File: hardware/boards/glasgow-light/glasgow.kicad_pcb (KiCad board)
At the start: 2 copper layers, 171 parts, among them J1 USB_C_USB2.0, J10 AUX, J2 IDC-Header_2x5_P2.54mm, J3 IDC-Header_2x5_P2.54mm, J4 Conn_01x02, U10 SN74LVC1T45DCKR, U11 SN74LVC1T45DCKR, U12 INA180A2, U15 TPD3S014, U16 SN74LVC1T45DCKR, U17 SN74LVC1T45DCKR, U18 SN74LVC1T45DCKR, U19 PCA6408APW, U31 TPS73101DBV, U36 TLV73312PQDRVR, U4 SN74LVC1T45DCKR, U5 ICE40UP5K-SG48ITR, U6 SN74LVC1T45DCKR, U7 GD32VF103, U8 TLV75533PDRVR, U9 SN74LVC1T45DCKR, Y1 8M

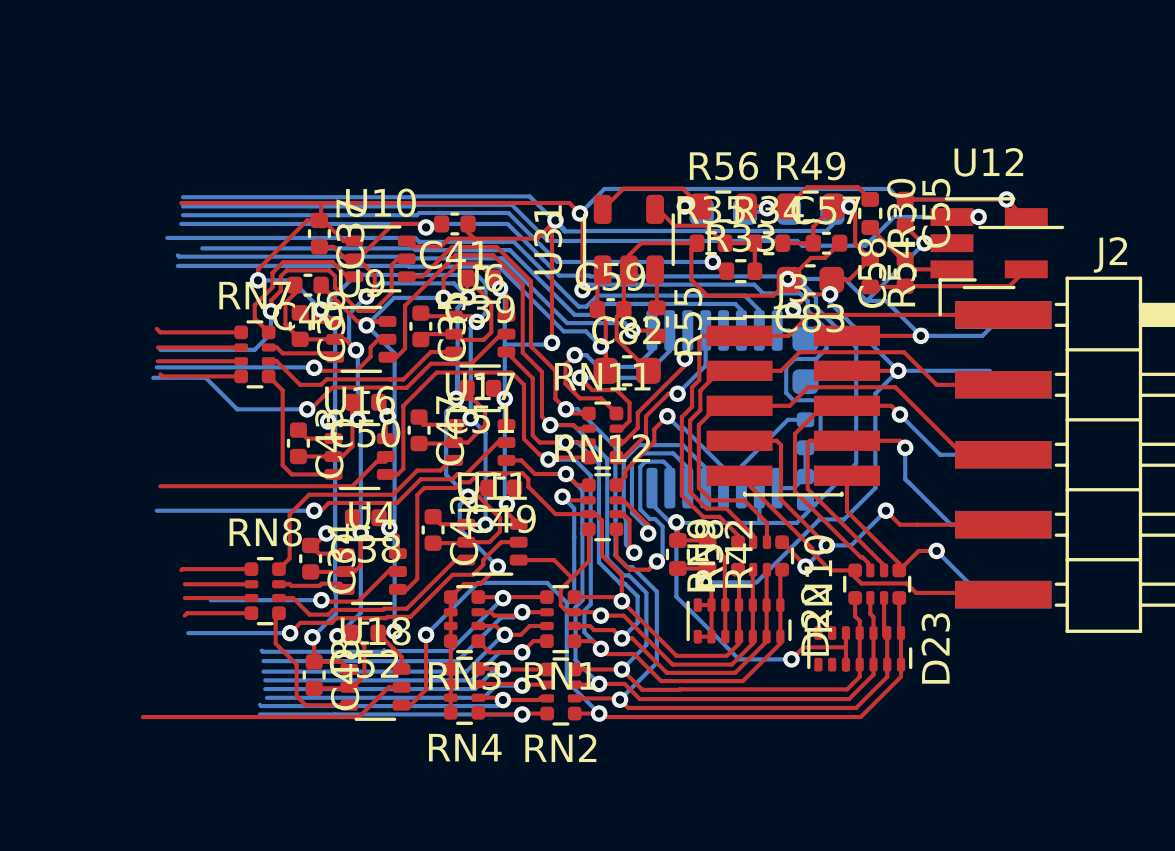
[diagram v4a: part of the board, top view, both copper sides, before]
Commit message: increase width of supply lines
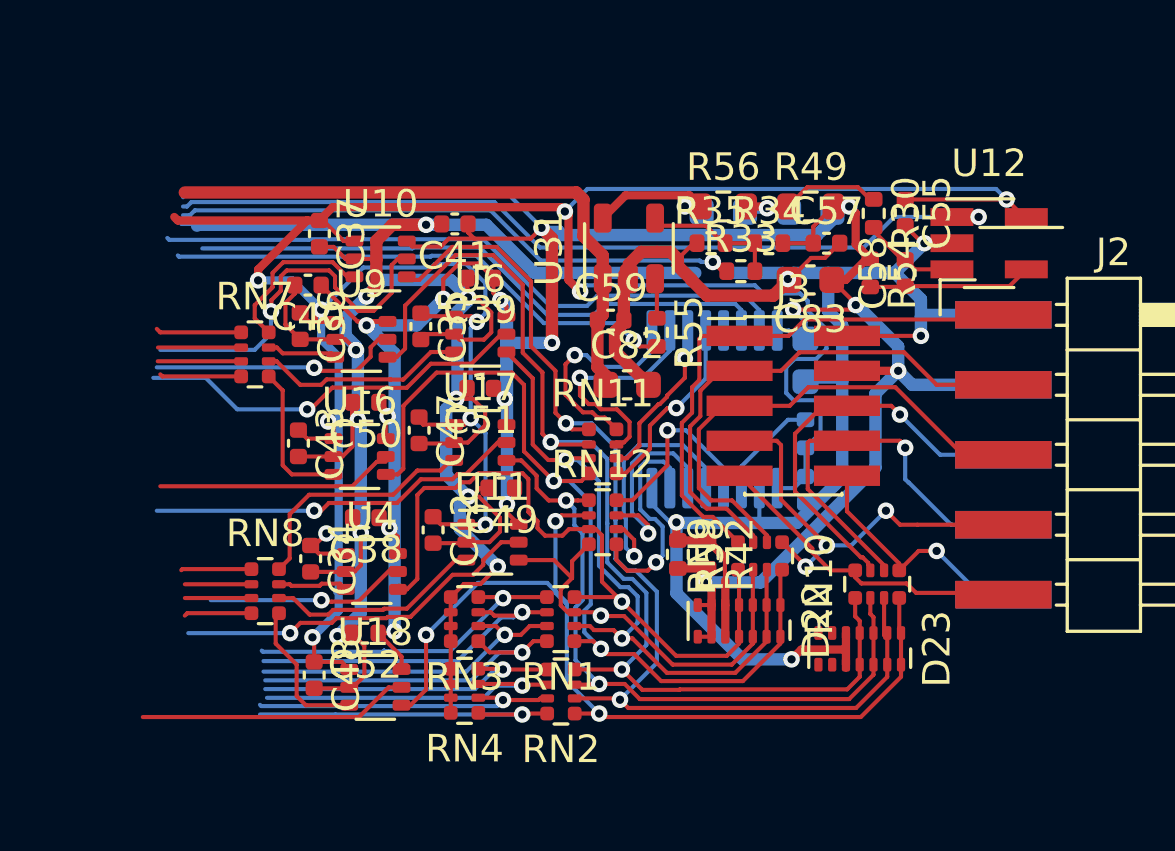
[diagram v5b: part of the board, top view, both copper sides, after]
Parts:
- moved RN11 0.58 mm to (157.4, 43.9)
- moved RN12 0.55 mm to (157.4, 46.5)
- moved C82 0.51 mm to (158.3, 41.5)
- moved C59 0.38 mm to (157.7, 39.2)
- moved R55 0.38 mm to (159.4, 39.6)
- moved U31 0.32 mm to (158.4, 36.6)
- moved R30 0.13 mm to (167.3, 35.3)
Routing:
- net /IO_Banks/VIOA: track 119.3 -> 150.2 mm
- net GND: track 169.1 -> 190.7 mm
- net +3V3: track 109.2 -> 115.3 mm
- net /IO_Banks/IO_Buffer_A/Y0: track 25.1 -> 25.9 mm
- net /IO_Banks/IO_Buffer_A/Y1: track 16.4 -> 15.7 mm
- net /IO_Banks/IO_Buffer_A/Y7: track 34.4 -> 33.7 mm
- net /IO_Banks/IO_Buffer_A/P6: track 5.28 -> 5.96 mm
- net /IO_Banks/IO_Buffer_A/P7: track 6.30 -> 6.91 mm
- net /IO_Banks/IO_Buffer_A/P5: track 7.83 -> 8.42 mm
- net +5V: track 21.4 -> 21.8 mm, vias 1 -> 0

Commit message: add some test points
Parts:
- removed D14: CDSOD323-T36S, Glasgow:D_SOD-323
- removed D5: RED, LED_SMD:LED_0603_1608Metric
- removed R13, R14: 20k, Resistor_SMD:R_0402_1005Metric
- removed R16: 10k, Resistor_SMD:R_0402_1005Metric
- added TP22: 3V3, TestPoint:TestPoint_Pad_D1.0mm, B.Cu at (172.5, 35.3)
- added TP23: VCURR, TestPoint:TestPoint_Pad_D1.0mm, B.Cu at (170.4, 35.3)
- added TP24: GND, TestPoint:TestPoint_Pad_D1.0mm, B.Cu at (170.4, 37.3)
- added TP25: VIO, TestPoint:TestPoint_Pad_D1.0mm, B.Cu at (172.5, 37.3)
- added TP26: Y5, TestPoint:TestPoint_Pad_D1.0mm, B.Cu at (160.0, 52.6)
- added TP27: Y6, TestPoint:TestPoint_Pad_D1.0mm, B.Cu at (160.0, 50.5)
- added TP28: Y7, TestPoint:TestPoint_Pad_D1.0mm, B.Cu at (162.1, 52.6)
- added TP29: ADC7, TestPoint:TestPoint_Pad_D1.0mm, B.Cu at (155.6, 53.2)
- added TP30: ADC5, TestPoint:TestPoint_Pad_D1.0mm, B.Cu at (155.3, 50.5)
- added TP31: GND, TestPoint:TestPoint_Pad_D1.0mm, B.Cu at (162.1, 50.5)
- added TP32: P5, TestPoint:TestPoint_Pad_D1.0mm, B.Cu at (157.9, 41.4)
- added TP33: P7, TestPoint:TestPoint_Pad_D1.0mm, B.Cu at (157.9, 43.4)
- TP4, TP5: moved to B.Cu
- moved J4 160.1 mm to (193.2, 103.5)
- moved J10 126.9 mm to (161.4, 110.9)
- moved TP5 119.8 mm to (155.4, 38.2)
- moved TP4 119.6 mm to (155.2, 41.3)
- moved R1 92.6 mm to (156.2, 39.1), turned to 90 degrees
- moved R2 90.9 mm to (155.8, 37.0), turned to 90 degrees
- moved R6 61.9 mm to (132.3, 87.4)
- moved C30 54.0 mm to (132.1, 83.6)
- moved C31 52.9 mm to (132.0, 79.1)
- moved C22 52.8 mm to (131.8, 74.7)
- moved C11 49.0 mm to (110.6, 53.5)
- moved C12 49.0 mm to (112.6, 57.3)
- moved R22 47.8 mm to (188.8, 75.8)
- moved R21 47.3 mm to (188.6, 63.6)
- moved C21 45.5 mm to (125.7, 85.7)
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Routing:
- net /IO_Banks/IO_Buffer_A/Y7: track 33.7 -> 38.9 mm
- net /IO_Banks/IO_Buffer_A/Y5: track 25.7 -> 29.1 mm
- net GND: track 190.7 -> 194.1 mm
- net /IO_Banks/VIOA: track 150.2 -> 153.2 mm, vias 15 -> 16
- net /SCL: track 21.6 -> 24.3 mm, vias 0 -> 2
- net /IO_Banks/IO_Buffer_A/P7: track 6.91 -> 9.58 mm
- net ADC5: track 12.0 -> 14.2 mm
- net +3V3: track 115.3 -> 117.0 mm
- net ADC7: track 12.1 -> 13.3 mm
- net VIO_CURRENT: track 31.1 -> 32.3 mm
- net /SDA: track 23.7 -> 24.3 mm, vias 0 -> 1

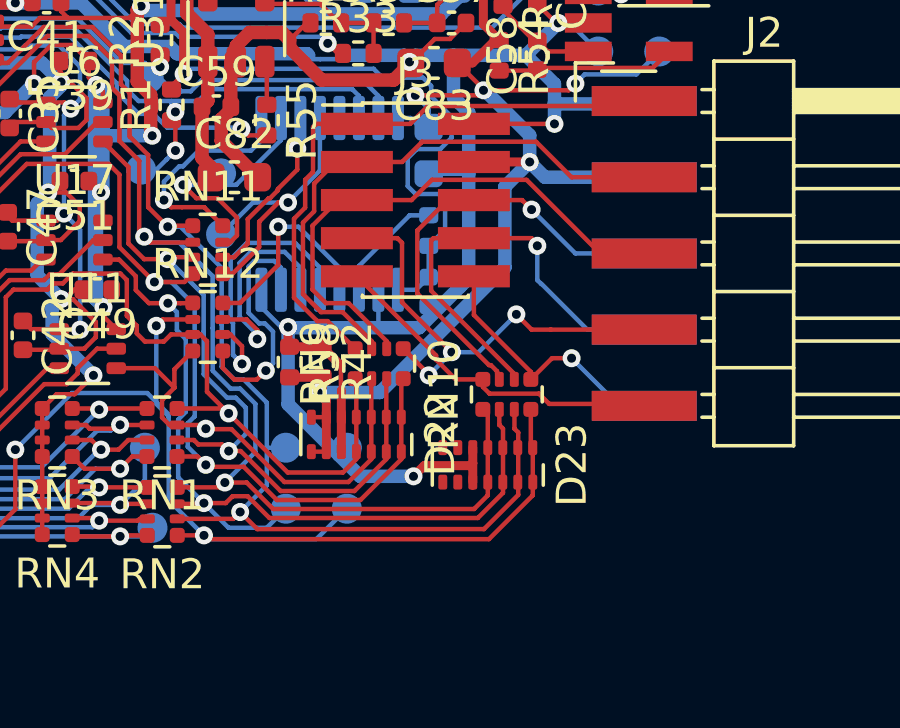
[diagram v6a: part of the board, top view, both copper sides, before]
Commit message: add LEDs for VIO and Y7
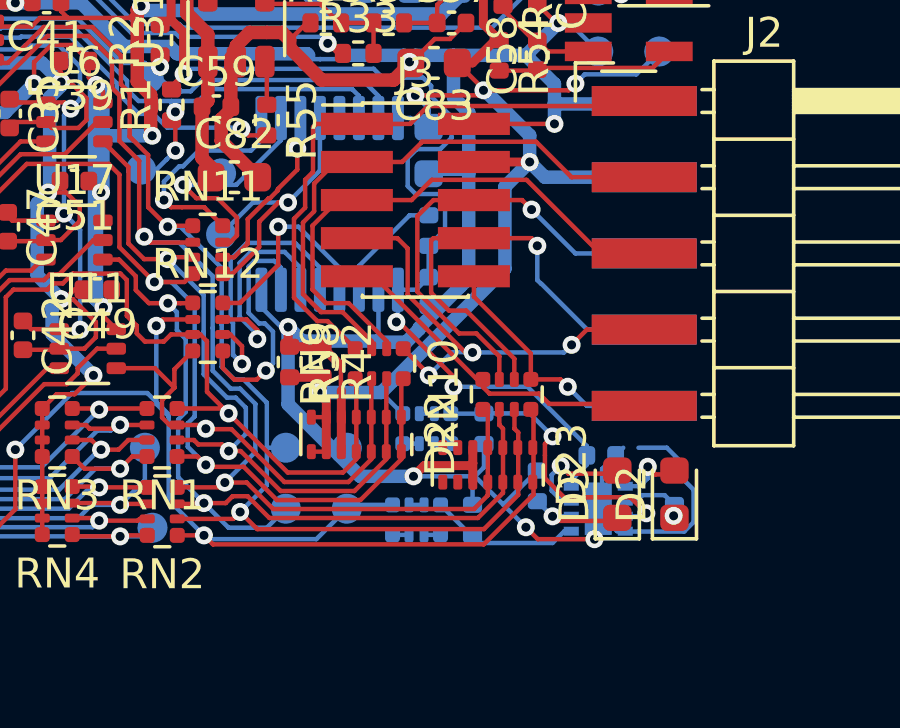
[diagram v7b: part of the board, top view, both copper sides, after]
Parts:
- added C32: u1, Capacitor_SMD:C_0402_1005Metric, B.Cu at (170.5, 50.8)
- added D2: GREEN, LED_SMD:LED_0603_1608Metric, F.Cu at (173.0, 52.1)
- added D3: YELLOW, LED_SMD:LED_0603_1608Metric, F.Cu at (171.1, 52.1)
- added R13: 50k, Resistor_SMD:R_0402_1005Metric, B.Cu at (166.6, 49.9)
- added R14: 50k, Resistor_SMD:R_0402_1005Metric, B.Cu at (166.2, 53.0)
- added R16: 270, Resistor_SMD:R_0402_1005Metric, B.Cu at (173.0, 51.9)
- added R19: 270, Resistor_SMD:R_0402_1005Metric, B.Cu at (168.4, 51.8)
- added RN5: 100k, Glasgow:R_Array_Convex_4x0402, B.Cu at (164.7, 49.9)
- added RN6: 100k, Glasgow:R_Array_Convex_4x0402, B.Cu at (164.4, 53.0)
- added U1: LM358_DFN, Package_DFN_QFN:DFN-8-1EP_2x2mm_P0.5mm_EP1.05x1.75mm, B.Cu at (170.4, 52.6)
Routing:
- net GND: track 194.1 -> 212.2 mm, vias 15 -> 17
- net +3V3: track 117.0 -> 127.9 mm, vias 11 -> 13
- net Net-(R13-Pad1): track 0.00 -> 9.71 mm, vias 0 -> 2
- net Net-(R14-Pad1): track 0.00 -> 5.05 mm
- net Net-(D3-Pad2): track 0.00 -> 3.62 mm, vias 0 -> 1
- net Net-(D3-Pad1): track 0.00 -> 3.44 mm, vias 0 -> 1
- net Net-(D2-Pad1): track 0.00 -> 2.47 mm, vias 0 -> 1
- net Net-(D2-Pad2): track 0.00 -> 2.24 mm, vias 0 -> 1
- net /IO_Banks/IO_Buffer_A/Y7: track 38.9 -> 40.7 mm
- net /IO_Banks/VIOA: track 153.2 -> 154.3 mm
- net /IO_Banks/IO_Buffer_A/Z7: track 8.95 -> 8.37 mm
- net /IO_Banks/IO_Buffer_A/Z5: track 14.9 -> 15.4 mm
- net Net-(RN6-Pad3): track 0.00 -> 0.55 mm
- net Net-(RN5-Pad1): track 0.00 -> 0.55 mm
- net Net-(RN6-Pad1): track 0.00 -> 0.55 mm
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
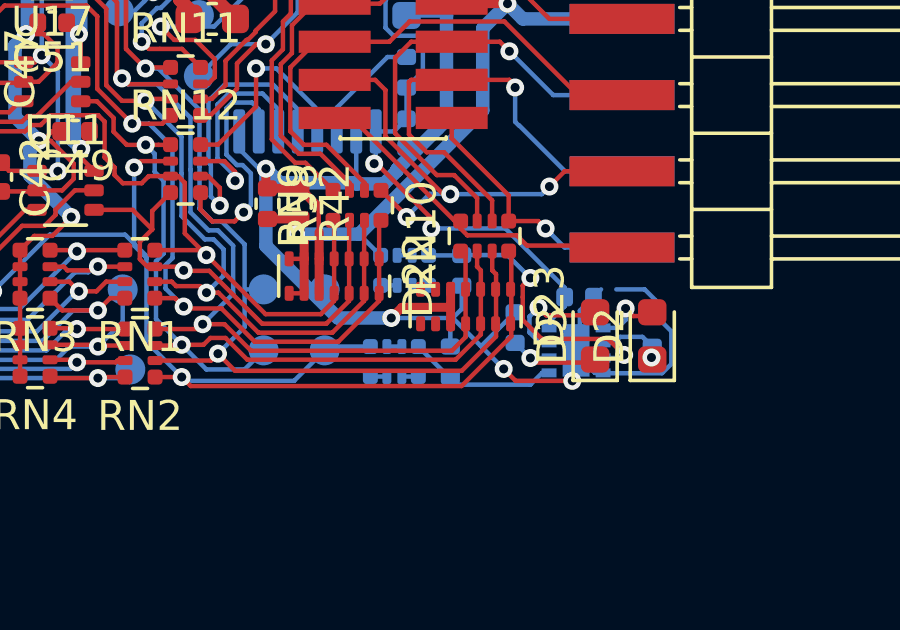
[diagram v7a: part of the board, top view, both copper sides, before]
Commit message: add alternative resistors
We might not want to place any resistor arrays on the bottom side
because we will most likely hand-solder it.
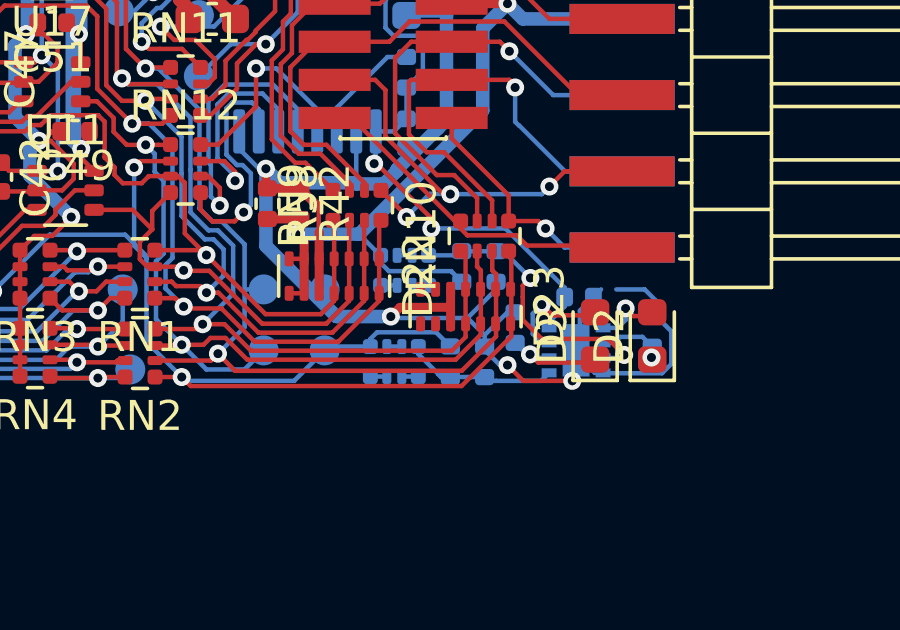
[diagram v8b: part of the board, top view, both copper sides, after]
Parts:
- added R24: DNP/400k, Resistor_SMD:R_0402_1005Metric, B.Cu at (166.6, 49.8)
- added R25: DNP/400k, Resistor_SMD:R_0402_1005Metric, B.Cu at (166.2, 53.0)
- moved R13 1.15 mm to (167.8, 49.8)
- moved R14 1.14 mm to (167.4, 53.0)
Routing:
- net /IO_Banks/VIOA: track 154.3 -> 157.5 mm
- net /IO_Banks/IO_Buffer_A/Y7: track 40.7 -> 43.9 mm
